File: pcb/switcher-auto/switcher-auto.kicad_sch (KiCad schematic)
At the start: 20 parts, among them J0 MD-90SM, J1 Conn_02x22_Top_Bottom, J2 Conn_02x22_Top_Bottom, J3 Conn_02x22_Top_Bottom, SW1 SW_Push, SW2 SW_Push, U1 CD74HC4067SM96, U2 CD74HC4067SM96, U3 CD74HC4067SM96, U4 CD74HC4067SM96, U5 CD74HC4067SM96, U6 CD74HC4067SM96, U7 CD74HC4067SM96

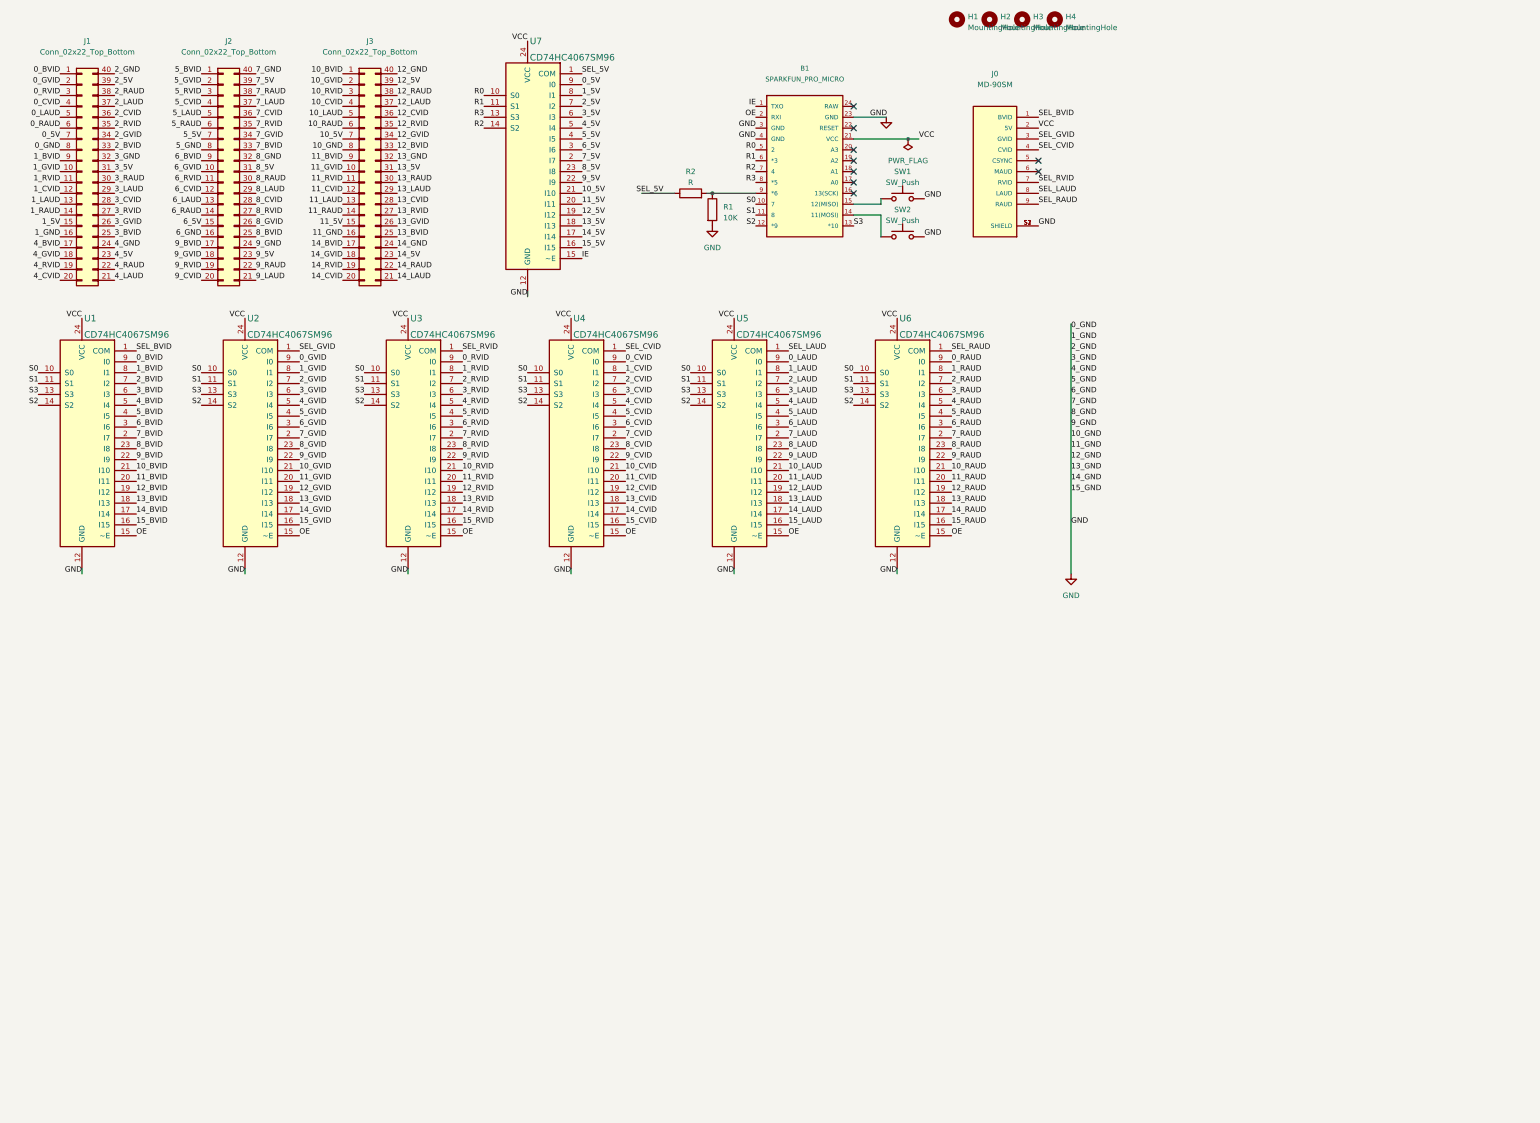
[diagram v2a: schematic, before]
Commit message: Merge schematics and fix connector mismatch
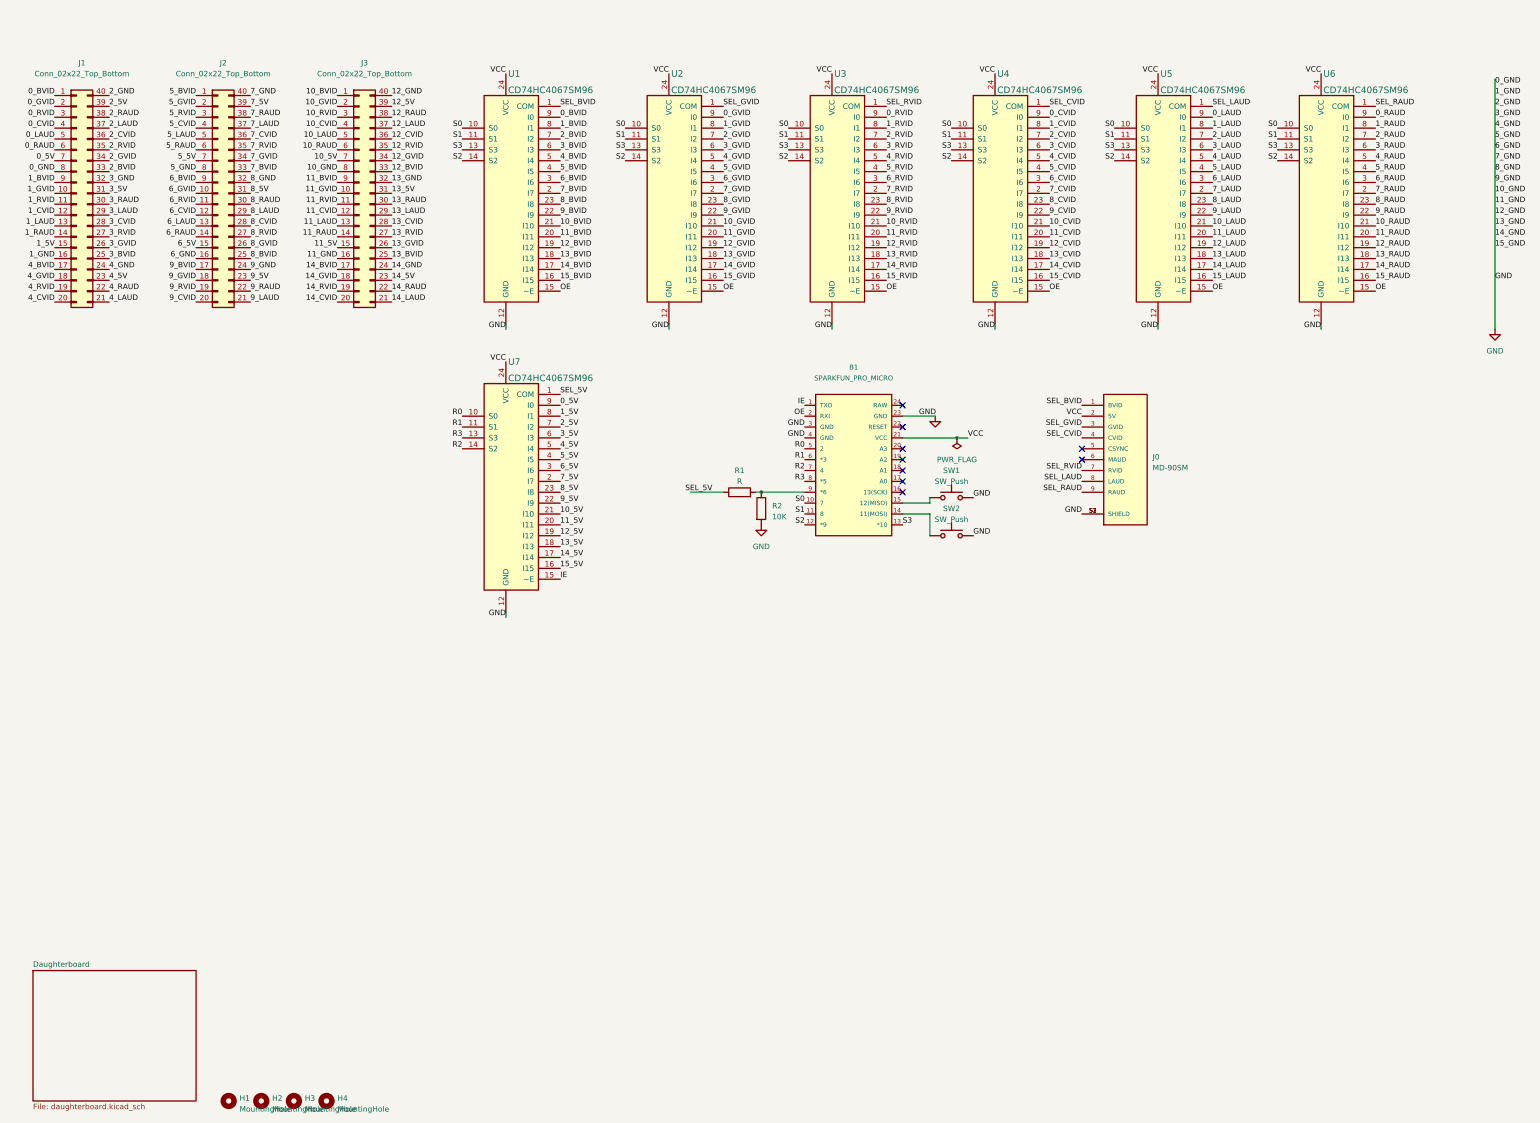
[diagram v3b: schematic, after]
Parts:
- renumbered R2 to R1, R1 to R2
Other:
- added sheet Daughterboard (daughterboard.kicad_sch)
- moved on the sheet: B1, H1, H2, H3, H4, J0, J1, J2, J3, R1, R2, SW1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

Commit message: WIP routing as 4 layers with new connector organization
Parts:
- removed J1, J2, J3: Conn_02x22_Top_Bottom, connector:REB_PinHeader_2x20_P1.27mm_Vertical_Renumbered, symbol Connector_Generic:Conn_02x20_Counter_Clockwise
- added J5 (x3): Conn_02x22_Top_Bottom, connector:REB_PinHeader_2x20_P1.27mm_Vertical_Renumbered, symbol Connector_Generic:Conn_02x20_Counter_Clockwise
- renumbered U3 to U1, U1 to U2, U2 to U3
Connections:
- net 0_BVID: now also J5.6 (Pin_6)
- net 0_CVID: now also J5.36 (Pin_36)
- net 0_GVID: now also J5.11 (Pin_11)
- net 0_LAUD: now also J5.31 (Pin_31)
- net 0_RAUD: now also J5.26 (Pin_26)
- net 0_RVID: now also J5.1 (Pin_1)
- net 10_BVID: now also J5.6 (Pin_6)
- net 10_CVID: now also J5.36 (Pin_36)
- net 10_GVID: now also J5.11 (Pin_11)
- net 10_LAUD: now also J5.31 (Pin_31)
- net 10_RAUD: now also J5.26 (Pin_26)
- net 10_RVID: now also J5.1 (Pin_1)
- net 11_BVID: now also J5.7 (Pin_7)
- net 11_CVID: now also J5.37 (Pin_37)
- net 11_GVID: now also J5.12 (Pin_12)
- net 11_LAUD: now also J5.32 (Pin_32)
- net 11_RAUD: now also J5.27 (Pin_27)
- net 11_RVID: now also J5.2 (Pin_2)
- net 12_BVID: now also J5.8 (Pin_8)
- net 12_CVID: now also J5.38 (Pin_38)
- net 12_GVID: now also J5.13 (Pin_13)
- net 12_LAUD: now also J5.33 (Pin_33)
- net 12_RAUD: now also J5.28 (Pin_28)
- net 12_RVID: now also J5.3 (Pin_3)
- net 13_BVID: now also J5.9 (Pin_9)
- net 13_CVID: now also J5.39 (Pin_39)
- net 13_GVID: now also J5.14 (Pin_14)
- net 13_LAUD: now also J5.34 (Pin_34)
- net 13_RAUD: now also J5.29 (Pin_29)
- net 13_RVID: now also J5.4 (Pin_4)
- net 14_BVID: now also J5.10 (Pin_10)
- net 14_CVID: now also J5.40 (Pin_40)
- net 14_GVID: now also J5.15 (Pin_15)
- net 14_LAUD: now also J5.35 (Pin_35)
- net 14_RAUD: now also J5.30 (Pin_30)
- net 14_RVID: now also J5.5 (Pin_5)
- net 1_BVID: now also J5.7 (Pin_7)
- net 1_CVID: now also J5.37 (Pin_37)
- net 1_GVID: now also J5.12 (Pin_12)
- net 1_LAUD: now also J5.32 (Pin_32)
- net 1_RAUD: now also J5.27 (Pin_27)
- net 1_RVID: now also J5.2 (Pin_2)
- net 2_BVID: now also J5.8 (Pin_8)
- net 2_CVID: now also J5.38 (Pin_38)
- net 2_GVID: now also J5.13 (Pin_13)
- net 2_LAUD: now also J5.33 (Pin_33)
- net 2_RAUD: now also J5.28 (Pin_28)
- net 2_RVID: now also J5.3 (Pin_3)
- net 3_BVID: now also J5.9 (Pin_9)
- net 3_CVID: now also J5.39 (Pin_39)
- net 3_GVID: now also J5.14 (Pin_14)
- net 3_LAUD: now also J5.34 (Pin_34)
- net 3_RAUD: now also J5.29 (Pin_29)
- net 3_RVID: now also J5.4 (Pin_4)
- net 4_BVID: now also J5.10 (Pin_10)
- net 4_CVID: now also J5.40 (Pin_40)
- net 4_GVID: now also J5.15 (Pin_15)
- net 4_LAUD: now also J5.35 (Pin_35)
- net 4_RAUD: now also J5.30 (Pin_30)
- net 4_RVID: now also J5.5 (Pin_5)
- net 5_BVID: now also J5.6 (Pin_6)
- net 5_CVID: now also J5.36 (Pin_36)
- net 5_GVID: now also J5.11 (Pin_11)
- net 5_LAUD: now also J5.31 (Pin_31)
- net 5_RAUD: now also J5.26 (Pin_26)
- net 5_RVID: now also J5.1 (Pin_1)
- net 6_BVID: now also J5.7 (Pin_7)
- net 6_CVID: now also J5.37 (Pin_37)
- net 6_GVID: now also J5.12 (Pin_12)
- net 6_LAUD: now also J5.32 (Pin_32)
- net 6_RAUD: now also J5.27 (Pin_27)
- net 6_RVID: now also J5.2 (Pin_2)
- net 7_BVID: now also J5.8 (Pin_8)
- net 7_CVID: now also J5.38 (Pin_38)
- net 7_GVID: now also J5.13 (Pin_13)
- net 7_LAUD: now also J5.33 (Pin_33)
- net 7_RAUD: now also J5.28 (Pin_28)
- net 7_RVID: now also J5.3 (Pin_3)
- net 8_BVID: now also J5.9 (Pin_9)
- net 8_CVID: now also J5.39 (Pin_39)
- net 8_GVID: now also J5.14 (Pin_14)
- net 8_LAUD: now also J5.34 (Pin_34)
- net 8_RAUD: now also J5.29 (Pin_29)
- net 8_RVID: now also J5.4 (Pin_4)
- net 9_BVID: now also J5.10 (Pin_10)
- net 9_CVID: now also J5.40 (Pin_40)
- net 9_GVID: now also J5.15 (Pin_15)
- net 9_LAUD: now also J5.35 (Pin_35)
- net 9_RAUD: now also J5.30 (Pin_30)
- net 9_RVID: now also J5.5 (Pin_5)
- net GND: now also J5.16 (Pin_16), J5.16 (Pin_16), J5.16 (Pin_16), J5.17 (Pin_17), J5.17 (Pin_17), J5.17 (Pin_17), J5.18 (Pin_18), J5.18 (Pin_18), J5.18 (Pin_18), J5.19 (Pin_19), J5.19 (Pin_19), J5.19 (Pin_19), J5.20 (Pin_20), J5.20 (Pin_20), J5.20 (Pin_20)
- net 0_5V renamed 0_VCC
- net 0_VCC: now also J5.21 (Pin_21)
- net 10_5V renamed 10_VCC
- net 10_VCC: now also J5.21 (Pin_21)
- net 11_5V renamed 11_VCC
- net 11_VCC: now also J5.22 (Pin_22)
- net 12_5V renamed 12_VCC
- net 12_VCC: now also J5.23 (Pin_23)
- net 13_5V renamed 13_VCC
- net 13_VCC: now also J5.24 (Pin_24)
- net 14_5V renamed 14_VCC
- net 14_VCC: now also J5.25 (Pin_25)
- net 15_5V renamed 15_VCC
- net 1_5V renamed 1_VCC
- net 1_VCC: now also J5.22 (Pin_22)
- net 2_5V renamed 2_VCC
- net 2_VCC: now also J5.23 (Pin_23)
- net 3_5V renamed 3_VCC
- net 3_VCC: now also J5.24 (Pin_24)
- net 4_5V renamed 4_VCC
- net 4_VCC: now also J5.25 (Pin_25)
- net 5_5V renamed 5_VCC
- net 5_VCC: now also J5.21 (Pin_21)
- net 6_5V renamed 6_VCC
- net 6_VCC: now also J5.22 (Pin_22)
- net 7_5V renamed 7_VCC
- net 7_VCC: now also J5.23 (Pin_23)
- net 8_5V renamed 8_VCC
- net 8_VCC: now also J5.24 (Pin_24)
- net 9_5V renamed 9_VCC
- net 9_VCC: now also J5.25 (Pin_25)
- net SEL_5V renamed SEL_VCC
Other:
- moved on the sheet: U1

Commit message: Routing pt 2
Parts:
- removed R1: R, Resistor_SMD:R_1206_3216Metric_Pad1.30x1.75mm_HandSolder, symbol Device:R
- removed R2: 10K, Resistor_SMD:R_1206_3216Metric_Pad1.30x1.75mm_HandSolder, symbol Device:R
- added C1: 1u, Capacitor_SMD:C_0805_2012Metric_Pad1.18x1.45mm_HandSolder, symbol Device:C_Small
- added R6: 10K, Resistor_SMD:R_0805_2012Metric_Pad1.20x1.40mm_HandSolder, symbol Device:R
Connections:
- net GND: now also U1.15 (~E), U2.15 (~E), U3.15 (~E), U4.15 (~E), U5.15 (~E), U6.15 (~E), C1.1, R6.2
- net R0: now also B1.6 (*3); no longer B1.5 (2)
- net R1: now also B1.5 (2); no longer B1.6 (*3)
- net R2: now also B1.8 (*5); no longer B1.7 (4)
- net R3: now also B1.7 (4); no longer B1.8 (*5)
- net SEL_VCC: now also B1.17 (A0), R6.1
- net VCC: now also C1.2
- net 15_BVID: no longer names the net of U2.16 (I15)
- net 15_CVID: no longer names the net of U4.16 (I15)
- net 15_GVID: no longer names the net of U3.16 (I15)
- net 15_LAUD: no longer names the net of U5.16 (I15)
- net 15_RAUD: no longer names the net of U6.16 (I15)
- net 15_RVID: no longer names the net of U1.16 (I15)
- net 15_VCC: no longer names the net of U7.16 (I15)
- removed net OE: B1.2 (RXI), U1.15 (~E), U2.15 (~E), U3.15 (~E), U4.15 (~E), U5.15 (~E), U6.15 (~E)
- no-connect marks 9 -> 17
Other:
- moved on the sheet: SW1, SW2

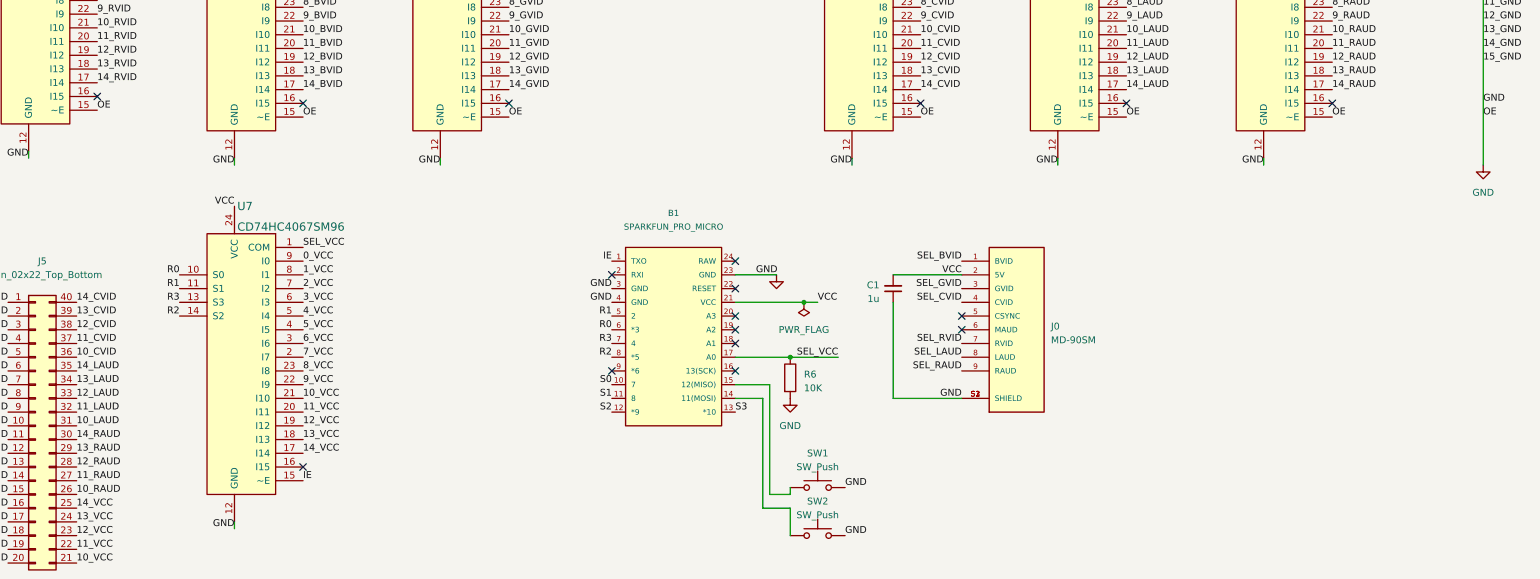
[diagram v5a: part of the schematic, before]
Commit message: Finish routing, not done with daughterboard changes
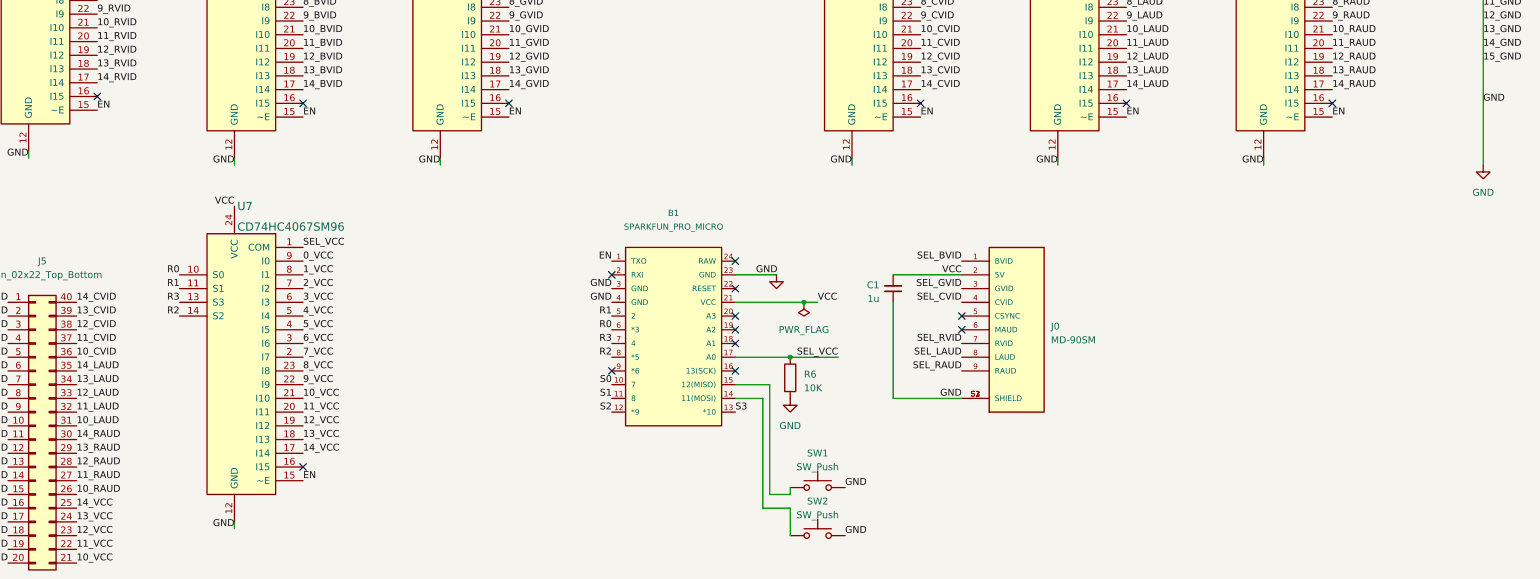
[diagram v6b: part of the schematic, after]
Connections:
- net GND: no longer U1.15 (~E), U2.15 (~E), U3.15 (~E), U4.15 (~E), U5.15 (~E), U6.15 (~E)
- net IE renamed EN
- net EN: now also U1.15 (~E), U2.15 (~E), U3.15 (~E), U4.15 (~E), U5.15 (~E), U6.15 (~E)
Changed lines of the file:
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@@
-    (stroke (width 0) (type default))
-  )
-  (wire (pts (xy 259.08 111.76) (xy 259.08 111.76))
     (stroke (width 0) (type default))
   )
@@
     (effects (font (size 1.27 1.27)) (justify right bottom))
   )
-  (label "OE" (at 111.76 81.28 0) (fields_autoplaced)
+  (label "EN" (at 111.76 81.28 0) (fields_autoplaced)
     (effects (font (size 1.27 1.27)) (justify left bottom))
   )
@@
     (effects (font (size 1.27 1.27)) (justify right bottom))
   )
-  (label "OE" (at 187.96 82.55 0) (fields_autoplaced)
+  (label "EN" (at 187.96 82.55 0) (fields_autoplaced)
     (effects (font (size 1.27 1.27)) (justify left bottom))
   )
@@
     (effects (font (size 1.27 1.27)) (justify left bottom))
   )
-  (label "OE" (at 368.3 82.55 0) (fields_autoplaced)
-    (effects (font (size 1.27 1.27)) (justify left bottom))
-  )
   (label "14_BVID" (at 149.86 77.47 0) (fields_autoplaced)
     (effects (font (size 1.27 1.27)) (justify left bottom))
@@
     (effects (font (size 1.27 1.27)) (justify left bottom))
   )
-  (label "IE" (at 149.86 149.86 0) (fields_autoplaced)
+  (label "EN" (at 149.86 149.86 0) (fields_autoplaced)
     (effects (font (size 1.27 1.27)) (justify left bottom))
   )
@@
     (effects (font (size 1.27 1.27)) (justify left bottom))
   )
-  (label "OE" (at 302.26 82.55 0) (fields_autoplaced)
+  (label "EN" (at 302.26 82.55 0) (fields_autoplaced)
     (effects (font (size 1.27 1.27)) (justify left bottom))
   )
@@
     (effects (font (size 1.27 1.27)) (justify left bottom))
   )
-  (label "OE" (at 264.16 82.55 0) (fields_autoplaced)
+  (label "EN" (at 264.16 82.55 0) (fields_autoplaced)
     (effects (font (size 1.27 1.27)) (justify left bottom))
   )
@@
     (effects (font (size 1.27 1.27)) (justify right bottom))
   )
-  (label "IE" (at 207.01 109.22 180) (fields_autoplaced)
+  (label "EN" (at 207.01 109.22 180) (fields_autoplaced)
     (effects (font (size 1.27 1.27)) (justify right bottom))
   )
@@
     (effects (font (size 1.27 1.27)) (justify right bottom))
   )
-  (label "OE" (at 149.86 82.55 0) (fields_autoplaced)
+  (label "EN" (at 149.86 82.55 0) (fields_autoplaced)
     (effects (font (size 1.27 1.27)) (justify left bottom))
   )
@@
     (effects (font (size 1.27 1.27)) (justify right bottom))
   )
-  (label "OE" (at 340.36 82.55 0) (fields_autoplaced)
-    (effects (font (size 1.27 1.27)) (justify left bottom))
-  )
+  (label "EN" (at 340.36 82.55 0) (fields_autoplaced)
+    (effects (font (size 1.27 1.27)) (justify left bottom))
+  )
